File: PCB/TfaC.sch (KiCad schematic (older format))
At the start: 0 parts

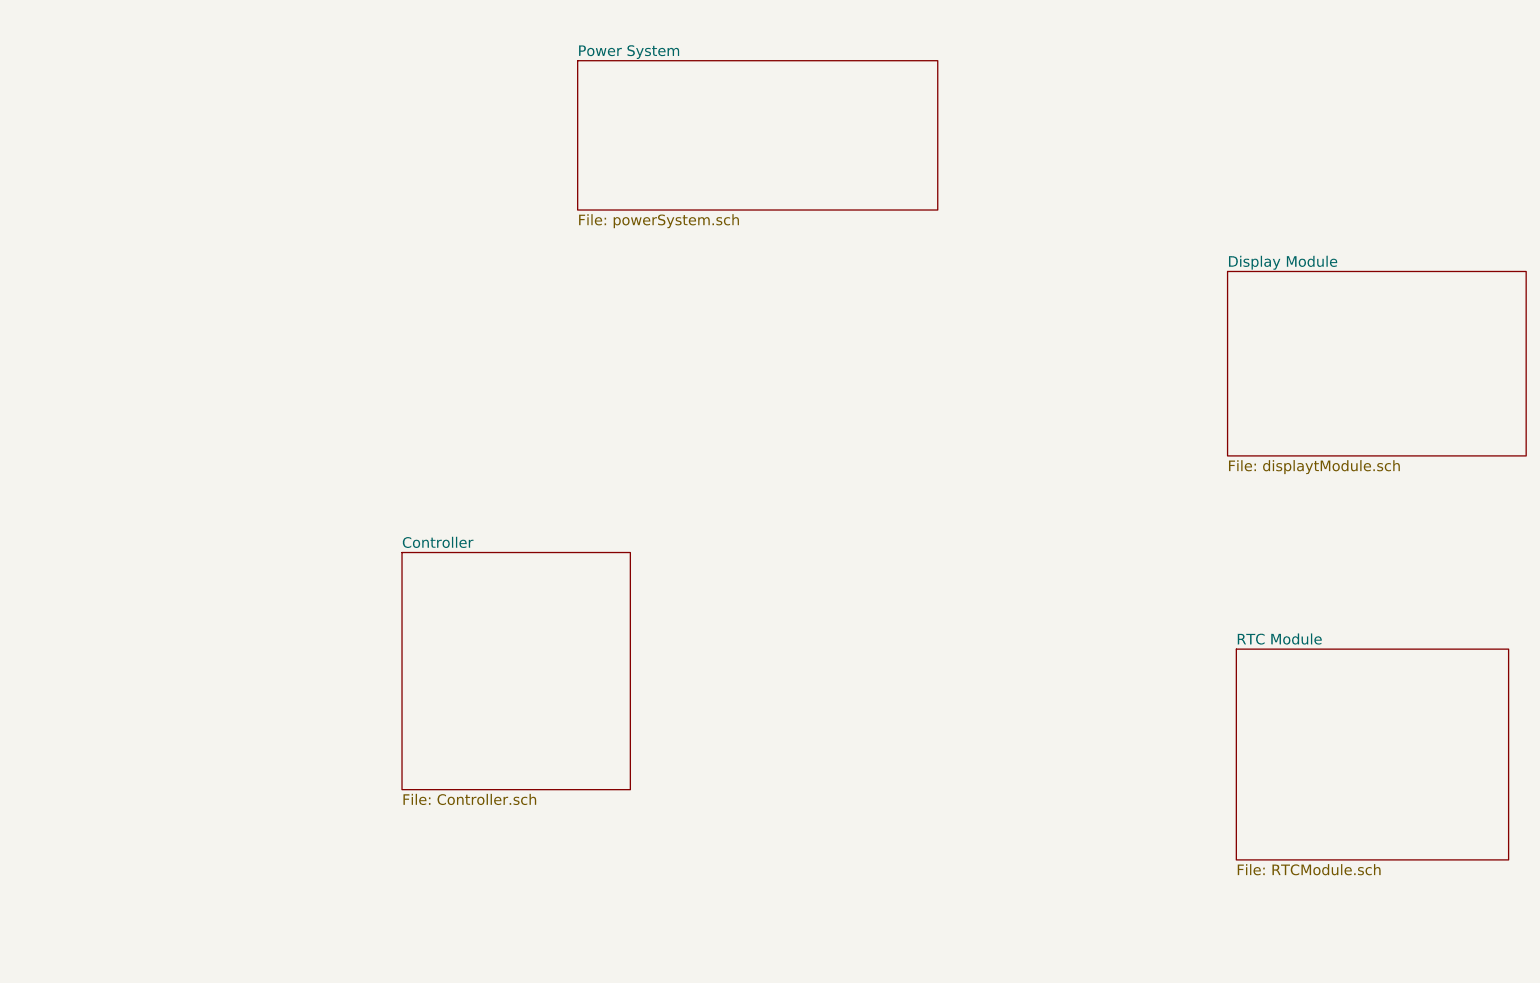
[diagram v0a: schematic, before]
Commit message: Started the schematic. Added the power circuit
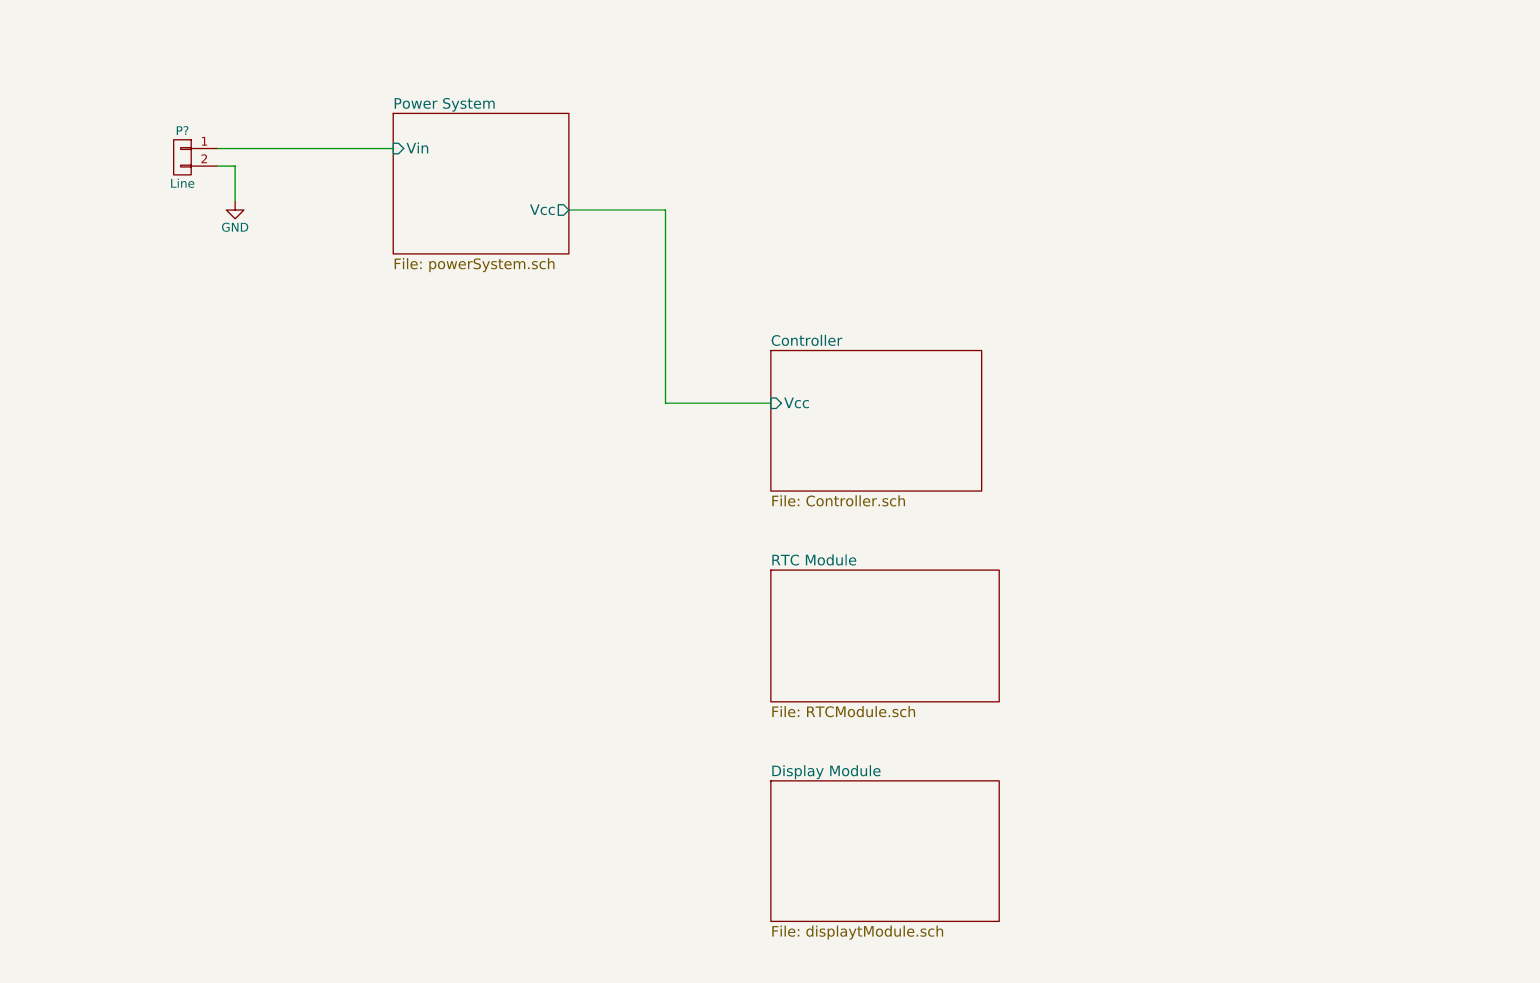
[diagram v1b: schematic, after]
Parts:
- added P?: Line, symbol CONN_01X02
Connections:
- new net GND: P?.2 (P2)
- new net Power System/Vin: P?.1 (P1)
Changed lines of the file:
@@
 LIBS:memory
 LIBS:xilinx
-LIBS:special
 LIBS:microcontrollers
 LIBS:dsp
@@
 LIBS:contrib
 LIBS:valves
+LIBS:Tfac-Symbols
+LIBS:TfaC-cache
 EELAYER 25 0
 EELAYER END
@@
 $EndDescr
 $Sheet
-S 4300 1000 2050 850
+S 3250 1300 1000 800
 U 5560D23E
 F0 "Power System" 60
 F1 "powerSystem.sch" 60
+F2 "Vin" I L 3250 1500 60
+F3 "Vcc" O R 4250 1850 60
 $EndSheet
 $Sheet
-S 3300 3800 1300 1350
+S 5400 2650 1200 800
 U 5560D274
 F0 "Controller" 60
 F1 "Controller.sch" 60
+F2 "Vcc" I L 5400 2950 60
 $EndSheet
 $Sheet
-S 8000 2200 1700 1050
+S 5400 5100 1300 800
 U 5560D289
 F0 "Display Module" 60
@@
 $EndSheet
 $Sheet
-S 8050 4350 1550 1200
+S 5400 3900 1300 750
 U 5560D2A4
 F0 "RTC Module" 60
 F1 "RTCModule.sch" 60
 $EndSheet
+$Comp
+L CONN_01X02 P?
+U 1 1 5565E10C
+P 2050 1550
+F 0 "P?" H 2050 1700 50  0000 C CNN
+F 1 "Line" H 2050 1400 50  0000 C CNN
+F 2 "" H 2050 1550 60  0000 C CNN
+F 3 "" H 2050 1550 60  0000 C CNN
+	1    2050 1550
+	-1   0    0    -1
+$EndComp
+Wire Wire Line
+	2250 1500 3250 1500
+$Comp
+L GND #PWR?
+U 1 1 5565E1CF
+P 2350 1800
+F 0 "#PWR?" H 2350 1550 50  0001 C CNN
+F 1 "GND" H 2350 1650 50  0000 C CNN
+F 2 "" H 2350 1800 60  0000 C CNN
+F 3 "" H 2350 1800 60  0000 C CNN
+	1    2350 1800
+	1    0    0    -1
+$EndComp
+Wire Wire Line
+	2250 1600 2350 1600
+Wire Wire Line
+	2350 1600 2350 1800
+Wire Wire Line
+	4250 1850 4800 1850
+Wire Wire Line
+	4800 1850 4800 2950
+Wire Wire Line
+	4800 2950 5400 2950
 $EndSCHEMATC

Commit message: Updated the schematic for the RTC and controller
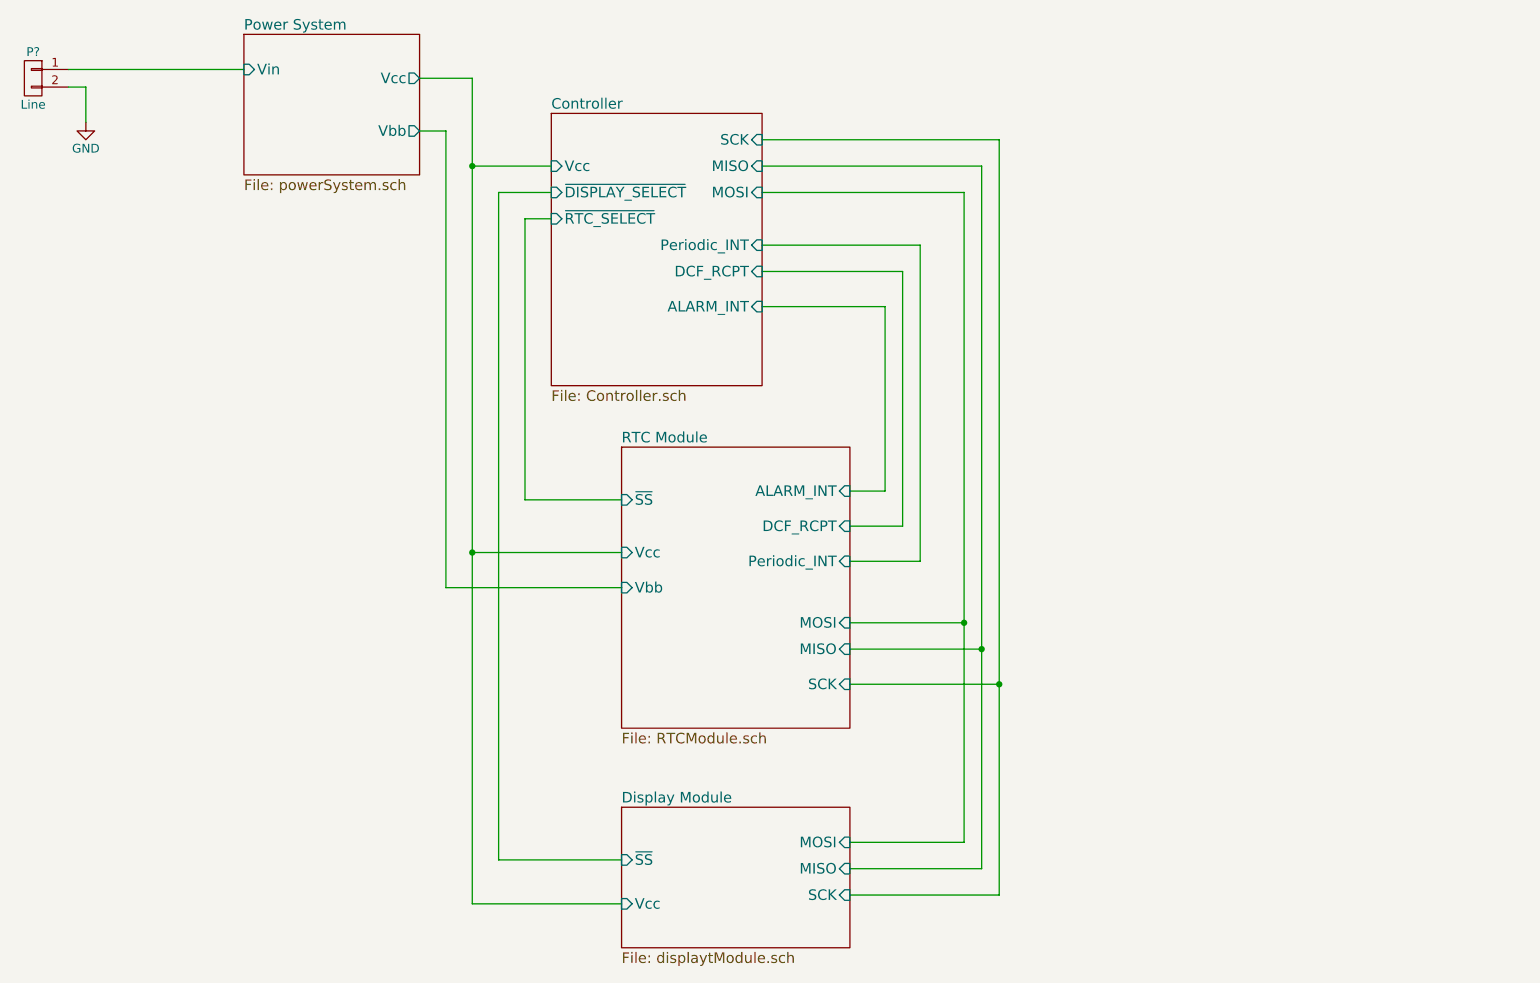
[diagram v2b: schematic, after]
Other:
- moved on the sheet: P?
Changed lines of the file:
@@
 $EndDescr
 $Sheet
-S 3250 1300 1000 800
+S 2400 850  1000 800
 U 5560D23E
 F0 "Power System" 60
 F1 "powerSystem.sch" 60
-F2 "Vin" I L 3250 1500 60
-F3 "Vcc" O R 4250 1850 60
+F2 "Vin" I L 2400 1050 60
+F3 "Vcc" O R 3400 1100 60
+F4 "Vbb" O R 3400 1400 60
 $EndSheet
 $Sheet
-S 5400 2650 1200 800
-U 5560D274
-F0 "Controller" 60
-F1 "Controller.sch" 60
-F2 "Vcc" I L 5400 2950 60
-$EndSheet
-$Sheet
-S 5400 5100 1300 800
+S 4550 5250 1300 800
 U 5560D289
 F0 "Display Module" 60
 F1 "displaytModule.sch" 60
+F2 "~SS" I L 4550 5550 60
+F3 "MISO" I R 5850 5600 60
+F4 "MOSI" I R 5850 5450 60
+F5 "SCK" I R 5850 5750 60
+F6 "Vcc" I L 4550 5800 60
 $EndSheet
 $Sheet
-S 5400 3900 1300 750
+S 4550 3200 1300 1600
 U 5560D2A4
 F0 "RTC Module" 60
 F1 "RTCModule.sch" 60
+F2 "Vbb" I L 4550 4000 60
+F3 "Vcc" I L 4550 3800 60
+F4 "~SS" I L 4550 3500 60
+F5 "MOSI" I R 5850 4200 60
+F6 "SCK" I R 5850 4550 60
+F7 "MISO" I R 5850 4350 60
+F8 "Periodic_INT" I R 5850 3850 60
+F9 "DCF_RCPT" I R 5850 3650 60
+F10 "ALARM_INT" I R 5850 3450 60
 $EndSheet
 $Comp
 L CONN_01X02 P?
 U 1 1 5565E10C
-P 2050 1550
-F 0 "P?" H 2050 1700 50  0000 C CNN
-F 1 "Line" H 2050 1400 50  0000 C CNN
-F 2 "" H 2050 1550 60  0000 C CNN
-F 3 "" H 2050 1550 60  0000 C CNN
-	1    2050 1550
+P 1200 1100
+F 0 "P?" H 1200 1250 50  0000 C CNN
+F 1 "Line" H 1200 950 50  0000 C CNN
+F 2 "" H 1200 1100 60  0000 C CNN
+F 3 "" H 1200 1100 60  0000 C CNN
+	1    1200 1100
 	-1   0    0    -1
 $EndComp
-Wire Wire Line
-	2250 1500 3250 1500
 $Comp
 L GND #PWR?
 U 1 1 5565E1CF
-P 2350 1800
-F 0 "#PWR?" H 2350 1550 50  0001 C CNN
-F 1 "GND" H 2350 1650 50  0000 C CNN
-F 2 "" H 2350 1800 60  0000 C CNN
-F 3 "" H 2350 1800 60  0000 C CNN
-	1    2350 1800
+P 1500 1350
+F 0 "#PWR?" H 1500 1100 50  0001 C CNN
+F 1 "GND" H 1500 1200 50  0000 C CNN
+F 2 "" H 1500 1350 60  0000 C CNN
+F 3 "" H 1500 1350 60  0000 C CNN
+	1    1500 1350
 	1    0    0    -1
 $EndComp
 Wire Wire Line
-	2250 1600 2350 1600
+	1400 1050 2400 1050
 Wire Wire Line
-	2350 1600 2350 1800
+	1400 1150 1500 1150
 Wire Wire Line
-	4250 1850 4800 1850
+	1500 1150 1500 1350
+$Sheet
+S 4150 1300 1200 1550
+U 5560D274
+F0 "Controller" 60
+F1 "Controller.sch" 60
+F2 "Vcc" I L 4150 1600 60
+F3 "MOSI" I R 5350 1750 60
+F4 "MISO" I R 5350 1600 60
+F5 "SCK" I R 5350 1450 60
+F6 "~DISPLAY_SELECT" I L 4150 1750 60
+F7 "~RTC_SELECT" I L 4150 1900 60
+F8 "Periodic_INT" I R 5350 2050 60
+F9 "DCF_RCPT" I R 5350 2200 60
+F10 "ALARM_INT" I R 5350 2400 60
+$EndSheet
 Wire Wire Line
-	4800 1850 4800 2950
+	5350 2050 6250 2050
 Wire Wire Line
-	4800 2950 5400 2950
+	6250 2050 6250 3850
+Wire Wire Line
+	6250 3850 5850 3850
+Wire Wire Line
+	5350 2200 6150 2200
+Wire Wire Line
+	6150 2200 6150 3650
+Wire Wire Line
+	6150 3650 5850 3650
+Wire Wire Line
+	5350 2400 6050 2400
+Wire Wire Line
+	6050 2400 6050 3450
+Wire Wire Line
+	6050 3450 5850 3450
+Wire Wire Line
+	3400 1100 3700 1100
+Wire Wire Line
+	3700 1100 3700 1600
+Wire Wire Line
+	3700 1600 3700 3800
+Wire Wire Line
+	3700 3800 3700 5800
+Wire Wire Line
+	3700 1600 4150 1600
+Wire Wire Line
+	3700 3800 4550 3800
+Connection ~ 3700 1600
+Wire Wire Line
+	3400 1400 3550 1400
+Wire Wire Line
+	3550 1400 3550 4000
+Wire Wire Line
+	3550 4000 4550 4000
+Wire Wire Line
+	3700 5800 4550 5800
+Connection ~ 3700 3800
+Wire Wire Line
+	4150 1750 3850 1750
+Wire Wire Line
+	3850 1750 3850 5550
+Wire Wire Line
+	3850 5550 4550 5550
+Wire Wire Line
+	4150 1900 4000 1900
+Wire Wire Line
+	4000 1900 4000 3500
+Wire Wire Line
+	4000 3500 4550 3500
+Wire Wire Line
+	5350 1750 6500 1750
+Wire Wire Line
+	6500 1750 6500 4200
+Wire Wire Line
+	6500 4200 6500 5450
+Wire Wire Line
+	6500 4200 5850 4200
+Wire Wire Line
+	5350 1600 6600 1600
+Wire Wire Line
+	6600 1600 6600 4350
+Wire Wire Line
+	6600 4350 6600 5600
+Wire Wire Line
+	6600 4350 5850 4350
+Wire Wire Line
+	5350 1450 6700 1450
+Wire Wire Line
+	6700 1450 6700 4550
+Wire Wire Line
+	6700 4550 6700 5750
+Wire Wire Line
+	6700 4550 5850 4550
+Wire Wire Line
+	6500 5450 5850 5450
+Connection ~ 6500 4200
+Wire Wire Line
+	6600 5600 5850 5600
+Connection ~ 6600 4350
+Wire Wire Line
+	6700 5750 5850 5750
+Connection ~ 6700 4550
 $EndSCHEMATC

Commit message: Generated the Netlist and started associating footprints
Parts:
- added ALMint1: ALMint, Pin_Headers:Pin_Header_Straight_1x01, symbol CONN_01X01
- added DCFint1: DCFint, Pin_Headers:Pin_Header_Straight_1x01, symbol CONN_01X01
- added TP-MISO1: MISO, Pin_Headers:Pin_Header_Straight_1x01, symbol CONN_01X01
- added TP-MOSI1: MOSI, Pin_Headers:Pin_Header_Straight_1x01, symbol CONN_01X01
- added TP-Pint1: Pint, Pin_Headers:Pin_Header_Straight_1x01, symbol CONN_01X01
- added TP-SCK1: SCK, Pin_Headers:Pin_Header_Straight_1x01, symbol CONN_01X01
- added TP-SS1: SS1, Pin_Headers:Pin_Header_Straight_1x01, symbol CONN_01X01
- added TP-SS2: SS2, Pin_Headers:Pin_Header_Straight_1x01, symbol CONN_01X01
- P101: renamed from P?; footprint (none) -> Pin_Headers:Pin_Header_Straight_1x02
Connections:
- wire segments 43 -> 40
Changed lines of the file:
@@
 LIBS:valves
 LIBS:Tfac-Symbols
+LIBS:TfaC-cache
 EELAYER 25 0
 EELAYER END
@@
 $EndSheet
 $Comp
-L CONN_01X02 P?
+L CONN_01X02 P101
 U 1 1 5565E10C
 P 1200 1100
-F 0 "P?" H 1200 1250 50  0000 C CNN
+F 0 "P101" H 1200 1250 50  0000 C CNN
 F 1 "Line" H 1200 950 50  0000 C CNN
-F 2 "" H 1200 1100 60  0000 C CNN
+F 2 "Pin_Headers:Pin_Header_Straight_1x02" H 1200 1100 60  0001 C CNN
 F 3 "" H 1200 1100 60  0000 C CNN
 	1    1200 1100
@@
 $EndComp
 $Comp
-L GND #PWR?
+L GND #PWR01
 U 1 1 5565E1CF
 P 1500 1350
-F 0 "#PWR?" H 1500 1100 50  0001 C CNN
+F 0 "#PWR01" H 1500 1100 50  0001 C CNN
 F 1 "GND" H 1500 1200 50  0000 C CNN
 F 2 "" H 1500 1350 60  0000 C CNN
@@
 	1    0    0    -1
 $EndComp
-Wire Wire Line
-	1400 1050 2400 1050
-Wire Wire Line
-	1400 1150 1500 1150
-Wire Wire Line
-	1500 1150 1500 1350
 $Sheet
 S 4150 1300 1200 1550
@@
 F10 "ALARM_INT" I R 5350 2400 60
 $EndSheet
-Wire Wire Line
-	5350 2050 6250 2050
+$Comp
+L CONN_01X01 TP-SCK1
+U 1 1 55C12D6C
+P 7150 1450
+F 0 "TP-SCK1" H 7150 1550 50  0000 C CNN
+F 1 "SCK" H 7300 1450 50  0000 C CNN
+F 2 "Pin_Headers:Pin_Header_Straight_1x01" H 7150 1450 60  0001 C CNN
+F 3 "" H 7150 1450 60  0000 C CNN
+	1    7150 1450
+	1    0    0    -1
+$EndComp
+$Comp
+L CONN_01X01 TP-MISO1
+U 1 1 55C13258
+P 7800 1600
+F 0 "TP-MISO1" H 7800 1700 50  0000 C CNN
+F 1 "MISO" H 7950 1600 50  0000 C CNN
+F 2 "Pin_Headers:Pin_Header_Straight_1x01" H 7800 1600 60  0001 C CNN
+F 3 "" H 7800 1600 60  0000 C CNN
+	1    7800 1600
+	1    0    0    -1
+$EndComp
+$Comp
+L CONN_01X01 TP-MOSI1
+U 1 1 55C1331B
+P 7150 1750
+F 0 "TP-MOSI1" H 7150 1850 50  0000 C CNN
+F 1 "MOSI" H 7300 1750 50  0000 C CNN
+F 2 "Pin_Headers:Pin_Header_Straight_1x01" H 7150 1750 60  0001 C CNN
+F 3 "" H 7150 1750 60  0000 C CNN
+	1    7150 1750
+	1    0    0    -1
+$EndComp
+$Comp
+L CONN_01X01 TP-SS1
+U 1 1 55C142EA
+P 4200 5100
+F 0 "TP-SS1" H 4200 5200 50  0000 C CNN
+F 1 "SS1" H 4350 5100 50  0000 C CNN
+F 2 "Pin_Headers:Pin_Header_Straight_1x01" H 4200 5100 60  0001 C CNN
+F 3 "" H 4200 5100 60  0000 C CNN
+	1    4200 5100
+	1    0    0    -1
+$EndComp
+$Comp
+L CONN_01X01 TP-SS2
+U 1 1 55C14795
+P 3200 3100
+F 0 "TP-SS2" H 3200 3200 50  0000 C CNN
+F 1 "SS2" H 3350 3100 50  0000 C CNN
+F 2 "Pin_Headers:Pin_Header_Straight_1x01" H 3200 3100 60  0001 C CNN
+F 3 "" H 3200 3100 60  0000 C CNN
+	1    3200 3100
+	-1   0    0    1
+$EndComp
+$Comp
+L CONN_01X01 TP-Pint1
+U 1 1 55C15931
+P 7150 2050
+F 0 "TP-Pint1" H 7150 2150 50  0000 C CNN
+F 1 "Pint" H 7300 2050 50  0000 C CNN
+F 2 "Pin_Headers:Pin_Header_Straight_1x01" H 7150 2050 60  0001 C CNN
+F 3 "" H 7150 2050 60  0000 C CNN
+	1    7150 2050
+	1    0    0    -1
+$EndComp
+$Comp
+L CONN_01X01 DCFint1
+U 1 1 55C15B52
+P 7650 2200
+F 0 "DCFint1" H 7650 2300 50  0000 C CNN
+F 1 "DCFint" H 7850 2200 50  0000 C CNN
+F 2 "Pin_Headers:Pin_Header_Straight_1x01" H 7650 2200 60  0001 C CNN
+F 3 "" H 7650 2200 60  0000 C CNN
+	1    7650 2200
+	1    0    0    -1
+$EndComp
+$Comp
+L CONN_01X01 ALMint1
+U 1 1 55C15C22
+P 7150 2400
+F 0 "ALMint1" H 7150 2500 50  0000 C CNN
+F 1 "ALMint" H 7350 2400 50  0000 C CNN
+F 2 "Pin_Headers:Pin_Header_Straight_1x01" H 7150 2400 60  0001 C CNN
+F 3 "" H 7150 2400 60  0000 C CNN
+	1    7150 2400
+	1    0    0    -1
+$EndComp
+Wire Wire Line
+	1400 1050 2400 1050
+Wire Wire Line
+	1400 1150 1500 1150
+Wire Wire Line
+	1500 1150 1500 1350
+Wire Wire Line
+	5350 2050 6950 2050
 Wire Wire Line
 	6250 2050 6250 3850
@@
 	6250 3850 5850 3850
 Wire Wire Line
-	5350 2200 6150 2200
+	5350 2200 7450 2200
 Wire Wire Line
 	6150 2200 6150 3650
@@
 	6150 3650 5850 3650
 Wire Wire Line
-	5350 2400 6050 2400
+	5350 2400 6950 2400
 Wire Wire Line
 	6050 2400 6050 3450
@@
 	3400 1100 3700 1100
 Wire Wire Line
-	3700 1100 3700 1600
-Wire Wire Line
-	3700 1600 3700 3800
-Wire Wire Line
-	3700 3800 3700 5800
+	3700 1100 3700 5800
 Wire Wire Line
 	3700 1600 4150 1600
@@
 	4000 3500 4550 3500
 Wire Wire Line
-	5350 1750 6500 1750
-Wire Wire Line
-	6500 1750 6500 4200
-Wire Wire Line
-	6500 4200 6500 5450
+	5350 1750 6950 1750
+Wire Wire Line
+	6500 1750 6500 5450
 Wire Wire Line
 	6500 4200 5850 4200
 Wire Wire Line
-	5350 1600 6600 1600
-Wire Wire Line
-	6600 1600 6600 4350
-Wire Wire Line
-	6600 4350 6600 5600
+	5350 1600 7600 1600
+Wire Wire Line
+	6600 1600 6600 5600
 Wire Wire Line
 	6600 4350 5850 4350
 Wire Wire Line
-	5350 1450 6700 1450
-Wire Wire Line
-	6700 1450 6700 4550
-Wire Wire Line
-	6700 4550 6700 5750
+	5350 1450 6950 1450
+Wire Wire Line
+	6700 1450 6700 5750
 Wire Wire Line
 	6700 4550 5850 4550
@@
 	6700 5750 5850 5750
 Connection ~ 6700 4550
+Wire Wire Line
+	3400 3100 4000 3100
+Connection ~ 4000 3100
+Wire Wire Line
+	4000 5100 3850 5100
+Connection ~ 3850 5100
+Connection ~ 6700 1450
+Connection ~ 6600 1600
+Connection ~ 6500 1750
+Connection ~ 6250 2050
+Connection ~ 6150 2200
+Connection ~ 6050 2400
 $EndSCHEMATC
